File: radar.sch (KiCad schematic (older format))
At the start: 4 parts

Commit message: Schematic finished
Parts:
- added C101, C104, C108, C110, C113: 10u, symbol C_Small
- added C102, C103, C105, C109, C111: 0u1, symbol C_Small
- added C106, C107: 22u, symbol C_Small
- added C112: 47u, symbol C_Small
- added J101, J102, J103, J104, J105: Conn_01x01, symbol Conn_01x01
- added J106, J107: Conn_01x02, symbol Conn_01x02
- added L101: 100u, symbol L_Small
- added R101: DNC, symbol R_Small
- added R102, R103: R_Small, symbol R_Small
- added U101: ADP150AUJZ-1.8-R7, symbol ADP150AUJZ-1.8-R7
- added U102: LM7805_TO220, TO_SOT_Packages_THT:TO-220_Vertical, symbol LM7805_TO220
- added U103: L78L33ABU, symbol L78L33ABU
- added U104: TPS54308, symbol TPS54308
- added U105: L4940D2T12-TR, symbol L4940D2T12-TR
- gave numbers to parts that had none: 4
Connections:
- net +12VA: now also C110.1, C111.1, R101.2, U105.3 (OUT)
- net +3V3: now also C104.1, C105.1, U101.1 (VIN), U101.3 (EN), U103.1 (VOUT)
- net +5V: now also C108.1, C109.1, U102.3 (VO)
- net +BATT: now also C112.1, C113.1, J107.1 (Pin_1), R101.1, U104.3 (VIN), U105.1 (IN)
- net BASEBAND/OUT: now also J105.1 (Pin_1)
- net POWER_AMP/EN: now also J103.1 (Pin_1)
- net POWER_AMP/PDET: now also J102.1 (Pin_1)
- net VCO/TUNE: now also J101.1 (Pin_1)
- net VCO/nEN: now also J104.1 (Pin_1)
- new net: C103.2, L101.1, U104.2 (SW)
- new net: R102.2, R103.1, U104.4 (FB)
- new net: C103.1, U104.6 (BOOT)
- new net: C106.1, C107.1, L101.2, R102.1, U102.1 (VI), U103.3 (VIN)
- new net +1V8: C101.1, C102.1, U101.5 (VOUT)
- new net GND: C101.2, C102.2, C104.2, C105.2, C106.2, C107.2, C108.2, C109.2, C110.2, C111.2, C112.2, C113.2, J107.2 (Pin_2), R103.2, U101.2 (GND), U102.2 (GND), U103.2 (GND), U104.1 (GND), U105.2 (GND)
- new net LEVELSHIFTER/IN1: J106.1 (Pin_1)
- new net LEVELSHIFTER/IN2: J106.2 (Pin_2)
- no-connect marks 0 -> 1
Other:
- note added: "0.7 A RMS, 0.75 A peak\n"
- moved on the sheet: AE101, AE102, T101, T102

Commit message: Assign a lot of footprints, fix l78l33abu part (input and output were reversed)
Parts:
- removed AE101, AE102: Antenna, symbol Antenna
- removed T101, T102: taper, symbol taper
- added J108, J109: Conn_Coaxial, symbol Conn_Coaxial
- C101, C104, C108, C110, C113: footprint (none) -> Capacitors_SMD:C_0805_HandSoldering
- C102, C103, C105, C109, C111: footprint (none) -> Capacitors_SMD:C_0603_HandSoldering
- C106, C107: footprint (none) -> Capacitors_SMD:C_1210_HandSoldering
- J101, J102, J103, J104, J105: footprint (none) -> Connectors:1pin
- J106, J107: footprint (none) -> Socket_Strips:Socket_Strip_Straight_1x02_Pitch2.54mm
- R101: footprint (none) -> Resistors_SMD:R_1206_HandSoldering
- R102: value R_Small -> 100k; footprint (none) -> Resistors_SMD:R_0402
- R103: value R_Small -> 10k; footprint (none) -> Resistors_SMD:R_0603_HandSoldering
- U101: footprint (none) -> rajsradar:TSOT-23
- U103: footprint (none) -> TO_SOT_Packages_SMD:SOT-89-3_Handsoldering
- U104: footprint (none) -> rajsradar:TI-SOT-23-6
- U105: footprint (none) -> rajsradar:D2PAK
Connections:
- net GND: now also J109.2 (Ext)
- net INPUT_AMP/RF_IN: now also J109.1 (In)
- net POWER_AMP/OUT: now also J108.1 (In)
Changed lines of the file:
@@
 Text Notes 6200 650  0    60   ~ 0
 +32 dB, 5V 600mA, max VSWR 4:1
-$Comp
-L Antenna AE101
-U 1 1 59D579C7
-P 8440 790
-F 0 "AE101" H 8365 865 50  0000 R CNN
-F 1 "Antenna" H 8365 790 50  0000 R CNN
-F 2 "" H 8440 790 50  0001 C CNN
-F 3 "" H 8440 790 50  0001 C CNN
-	1    8440 790
-	1    0    0    -1
-$EndComp
-$Comp
-L taper T101
-U 1 1 59D57BA6
-P 8000 1190
-F 0 "T101" H 8000 1340 60  0000 C CNN
-F 1 "taper" H 7900 1040 60  0000 C CNN
-F 2 "" H 8000 1190 60  0001 C CNN
-F 3 "" H 8000 1190 60  0001 C CNN
-	1    8000 1190
-	-1   0    0    1
-$EndComp
 $Sheet
 S 6240 1840 1130 1260
@@
 F4 "OUT" I R 9000 2410 60
 $EndSheet
-$Comp
-L Antenna AE102
-U 1 1 59D63482
-P 2020 2410
-F 0 "AE102" H 1945 2485 50  0000 R CNN
-F 1 "Antenna" H 1945 2410 50  0000 R CNN
-F 2 "" H 2020 2410 50  0001 C CNN
-F 3 "" H 2020 2410 50  0001 C CNN
-	1    2020 2410
-	-1   0    0    -1
-$EndComp
-$Comp
-L taper T102
-U 1 1 59D63488
-P 2460 2810
-F 0 "T102" H 2460 2960 60  0000 C CNN
-F 1 "taper" H 2360 2660 60  0000 C CNN
-F 2 "" H 2460 2810 60  0001 C CNN
-F 3 "" H 2460 2810 60  0001 C CNN
-	1    2460 2810
-	1    0    0    1
-$EndComp
 Text Notes 6360 3290 0    60   ~ 0
 +0 dB, 5V 60mA
@@
 F 0 "R101" H 2150 4880 50  0000 L CNN
 F 1 "DNC" H 2150 4820 50  0000 L CNN
-F 2 "" H 2120 4860 50  0001 C CNN
+F 2 "Resistors_SMD:R_1206_HandSoldering" H 2120 4860 50  0001 C CNN
 F 3 "" H 2120 4860 50  0001 C CNN
 	1    2120 4860
@@
 F 0 "U105" H 2130 5170 60  0000 C CNN
 F 1 "L4940D2T12-TR" H 2130 5320 60  0000 C CNN
-F 2 "" H 2130 5170 60  0001 C CNN
+F 2 "rajsradar:D2PAK" H 2130 5170 60  0001 C CNN
 F 3 "" H 2130 5170 60  0001 C CNN
 	1    2130 5170
@@
 F 0 "U104" H 3890 4900 60  0000 C CNN
 F 1 "TPS54308" H 3890 5200 60  0000 C CNN
-F 2 "" H 3890 4900 60  0001 C CNN
+F 2 "rajsradar:TI-SOT-23-6" H 3890 4900 60  0001 C CNN
 F 3 "" H 3890 4900 60  0001 C CNN
 	1    3890 4900
@@
 F 0 "C103" H 4630 4820 50  0000 L CNN
 F 1 "0u1" H 4630 4670 50  0000 L CNN
-F 2 "" H 4620 4750 50  0001 C CNN
+F 2 "Capacitors_SMD:C_0603_HandSoldering" H 4620 4750 50  0001 C CNN
 F 3 "" H 4620 4750 50  0001 C CNN
 	1    4620 4750
@@
 F 0 "C106" H 5090 5110 50  0000 L CNN
 F 1 "22u" H 5090 4960 50  0000 L CNN
-F 2 "" H 5080 5040 50  0001 C CNN
+F 2 "Capacitors_SMD:C_1210_HandSoldering" H 5080 5040 50  0001 C CNN
 F 3 "" H 5080 5040 50  0001 C CNN
 	1    5080 5040
@@
 F 0 "C107" H 5300 5110 50  0000 L CNN
 F 1 "22u" H 5300 4960 50  0000 L CNN
-F 2 "" H 5290 5040 50  0001 C CNN
+F 2 "Capacitors_SMD:C_1210_HandSoldering" H 5290 5040 50  0001 C CNN
 F 3 "" H 5290 5040 50  0001 C CNN
 	1    5290 5040
@@
 P 5540 5050
 F 0 "R102" H 5570 5070 50  0000 L CNN
-F 1 "R_Small" H 5570 5010 50  0000 L CNN
-F 2 "" H 5540 5050 50  0001 C CNN
+F 1 "100k" H 5570 5010 50  0000 L CNN
+F 2 "Resistors_SMD:R_0402" H 5540 5050 50  0001 C CNN
 F 3 "" H 5540 5050 50  0001 C CNN
 	1    5540 5050
@@
 P 5540 5300
 F 0 "R103" H 5570 5320 50  0000 L CNN
-F 1 "R_Small" H 5570 5260 50  0000 L CNN
-F 2 "" H 5540 5300 50  0001 C CNN
+F 1 "10k" H 5570 5260 50  0000 L CNN
+F 2 "Resistors_SMD:R_0603_HandSoldering" H 5540 5300 50  0001 C CNN
 F 3 "" H 5540 5300 50  0001 C CNN
 	1    5540 5300
@@
 F 0 "C110" H 2770 5410 50  0000 L CNN
 F 1 "10u" H 2770 5260 50  0000 L CNN
-F 2 "" H 2760 5340 50  0001 C CNN
+F 2 "Capacitors_SMD:C_0805_HandSoldering" H 2760 5340 50  0001 C CNN
 F 3 "" H 2760 5340 50  0001 C CNN
 	1    2760 5340
@@
 F 0 "C111" H 2980 5410 50  0000 L CNN
 F 1 "0u1" H 2980 5260 50  0000 L CNN
-F 2 "" H 2970 5340 50  0001 C CNN
+F 2 "Capacitors_SMD:C_0603_HandSoldering" H 2970 5340 50  0001 C CNN
 F 3 "" H 2970 5340 50  0001 C CNN
 	1    2970 5340
@@
 F 0 "C113" H 1550 5440 50  0000 L CNN
 F 1 "10u" H 1550 5290 50  0000 L CNN
-F 2 "" H 1540 5370 50  0001 C CNN
+F 2 "Capacitors_SMD:C_0805_HandSoldering" H 1540 5370 50  0001 C CNN
 F 3 "" H 1540 5370 50  0001 C CNN
 	1    1540 5370
@@
 F 0 "U103" H 7250 4780 60  0000 C CNN
 F 1 "L78L33ABU" H 7250 4880 60  0000 C CNN
-F 2 "" H 7250 4630 60  0001 C CNN
+F 2 "TO_SOT_Packages_SMD:SOT-89-3_Handsoldering" H 7250 4630 60  0001 C CNN
 F 3 "" H 7250 4630 60  0001 C CNN
 	1    7250 4630
@@
 F 0 "U101" H 8880 4480 60  0000 C CNN
 F 1 "ADP150AUJZ-1.8-R7" H 8880 4680 60  0000 C CNN
-F 2 "" H 8880 4480 60  0001 C CNN
+F 2 "rajsradar:TSOT-23" H 8880 4480 60  0001 C CNN
 F 3 "" H 8880 4480 60  0001 C CNN
 	1    8880 4480
@@
 F 0 "C108" H 6410 5160 50  0000 L CNN
 F 1 "10u" H 6410 5010 50  0000 L CNN
-F 2 "" H 6400 5090 50  0001 C CNN
+F 2 "Capacitors_SMD:C_0805_HandSoldering" H 6400 5090 50  0001 C CNN
 F 3 "" H 6400 5090 50  0001 C CNN
 	1    6400 5090
@@
 F 0 "C109" H 6620 5160 50  0000 L CNN
 F 1 "0u1" H 6620 5010 50  0000 L CNN
-F 2 "" H 6610 5090 50  0001 C CNN
+F 2 "Capacitors_SMD:C_0603_HandSoldering" H 6610 5090 50  0001 C CNN
 F 3 "" H 6610 5090 50  0001 C CNN
 	1    6610 5090
@@
 F 0 "C104" H 7790 4870 50  0000 L CNN
 F 1 "10u" H 7790 4720 50  0000 L CNN
-F 2 "" H 7780 4800 50  0001 C CNN
+F 2 "Capacitors_SMD:C_0805_HandSoldering" H 7780 4800 50  0001 C CNN
 F 3 "" H 7780 4800 50  0001 C CNN
 	1    7780 4800
@@
 F 0 "C105" H 8000 4870 50  0000 L CNN
 F 1 "0u1" H 8000 4720 50  0000 L CNN
-F 2 "" H 7990 4800 50  0001 C CNN
+F 2 "Capacitors_SMD:C_0603_HandSoldering" H 7990 4800 50  0001 C CNN
 F 3 "" H 7990 4800 50  0001 C CNN
 	1    7990 4800
@@
 F 0 "C101" H 9570 4670 50  0000 L CNN
 F 1 "10u" H 9570 4520 50  0000 L CNN
-F 2 "" H 9560 4600 50  0001 C CNN
+F 2 "Capacitors_SMD:C_0805_HandSoldering" H 9560 4600 50  0001 C CNN
 F 3 "" H 9560 4600 50  0001 C CNN
 	1    9560 4600
@@
 F 0 "C102" H 9780 4670 50  0000 L CNN
 F 1 "0u1" H 9780 4520 50  0000 L CNN
-F 2 "" H 9770 4600 50  0001 C CNN
+F 2 "Capacitors_SMD:C_0603_HandSoldering" H 9770 4600 50  0001 C CNN
 F 3 "" H 9770 4600 50  0001 C CNN
 	1    9770 4600
@@
 	5380 2790 6240 2790
 Wire Wire Line
-	2760 2810 3200 2810
-Wire Wire Line
-	2020 2810 2160 2810
-Wire Wire Line
-	2020 2610 2020 2810
+	1740 2470 3200 2470
 Wire Wire Line
 	5520 1930 6240 1930
 Wire Wire Line
-	7700 1190 7370 1190
-Wire Wire Line
-	8440 1190 8300 1190
-Wire Wire Line
-	8440 990  8440 1190
+	7370 1190 8440 1190
 Wire Wire Line
 	5520 1260 6240 1260
@@
 $EndSheet
 Wire Wire Line
-	3200 2810 3200 3100
+	3200 2470 3200 3100
 Wire Wire Line
 	3200 3100 3290 3100
@@
 F 0 "J106" H 1010 3480 50  0000 C CNN
 F 1 "Conn_01x02" H 1010 3180 50  0000 C CNN
-F 2 "" H 1010 3380 50  0001 C CNN
+F 2 "Socket_Strips:Socket_Strip_Straight_1x02_Pitch2.54mm" H 1010 3380 50  0001 C CNN
 F 3 "" H 1010 3380 50  0001 C CNN
 	1    1010 3380
@@
 F 0 "J104" H 2620 1820 50  0000 C CNN
 F 1 "Conn_01x01" H 2620 1620 50  0000 C CNN
-F 2 "" H 2620 1720 50  0001 C CNN
+F 2 "Connectors:1pin" H 2620 1720 50  0001 C CNN
 F 3 "" H 2620 1720 50  0001 C CNN
 	1    2620 1720
@@
 F 0 "J101" H 2600 1390 50  0000 C CNN
 F 1 "Conn_01x01" H 2600 1190 50  0000 C CNN
-F 2 "" H 2600 1290 50  0001 C CNN
+F 2 "Connectors:1pin" H 2600 1290 50  0001 C CNN
 F 3 "" H 2600 1290 50  0001 C CNN
 	1    2600 1290
@@
 F 0 "J103" H 5810 1550 50  0000 C CNN
 F 1 "Conn_01x01" H 5810 1350 50  0000 C CNN
-F 2 "" H 5810 1450 50  0001 C CNN
+F 2 "Connectors:1pin" H 5810 1450 50  0001 C CNN
 F 3 "" H 5810 1450 50  0001 C CNN
 	1    5810 1450
@@
 F 0 "J102" H 7720 1520 50  0000 C CNN
 F 1 "Conn_01x01" H 7720 1320 50  0000 C CNN
-F 2 "" H 7720 1420 50  0001 C CNN
+F 2 "Connectors:1pin" H 7720 1420 50  0001 C CNN
 F 3 "" H 7720 1420 50  0001 C CNN
 	1    7720 1420
@@
 F 0 "J105" H 9330 2510 50  0000 C CNN
 F 1 "Conn_01x01" H 9330 2310 50  0000 C CNN
-F 2 "" H 9330 2410 50  0001 C CNN
+F 2 "Connectors:1pin" H 9330 2410 50  0001 C CNN
 F 3 "" H 9330 2410 50  0001 C CNN
 	1    9330 2410
@@
 F 0 "J107" H 700 4740 50  0000 C CNN
 F 1 "Conn_01x02" H 700 4440 50  0000 C CNN
-F 2 "" H 700 4640 50  0001 C CNN
+F 2 "Socket_Strips:Socket_Strip_Straight_1x02_Pitch2.54mm" H 700 4640 50  0001 C CNN
 F 3 "" H 700 4640 50  0001 C CNN
 	1    700  4640
@@
 Wire Wire Line
 	1020 4740 900  4740
+$Comp
+L Conn_Coaxial J109
+U 1 1 5A5A7286
+P 1590 2470
+F 0 "J109" H 1600 2590 50  0000 C CNN
+F 1 "Conn_Coaxial" V 1705 2470 50  0000 C CNN
+F 2 "" H 1590 2470 50  0001 C CNN
+F 3 "" H 1590 2470 50  0001 C CNN
+	1    1590 2470
+	-1   0    0    -1
+$EndComp
+$Comp
+L Conn_Coaxial J108
+U 1 1 5A5A73C3
+P 8590 1190
+F 0 "J108" H 8600 1310 50  0000 C CNN
+F 1 "Conn_Coaxial" V 8705 1190 50  0000 C CNN
+F 2 "" H 8590 1190 50  0001 C CNN
+F 3 "" H 8590 1190 50  0001 C CNN
+	1    8590 1190
+	1    0    0    -1
+$EndComp
+$Comp
+L GND #PWR025
+U 1 1 5A5A8BA4
+P 1590 2760
+F 0 "#PWR025" H 1590 2510 50  0001 C CNN
+F 1 "GND" H 1590 2610 50  0000 C CNN
+F 2 "" H 1590 2760 50  0001 C CNN
+F 3 "" H 1590 2760 50  0001 C CNN
+	1    1590 2760
+	1    0    0    -1
+$EndComp
+Wire Wire Line
+	1590 2670 1590 2760
 $EndSCHEMATC

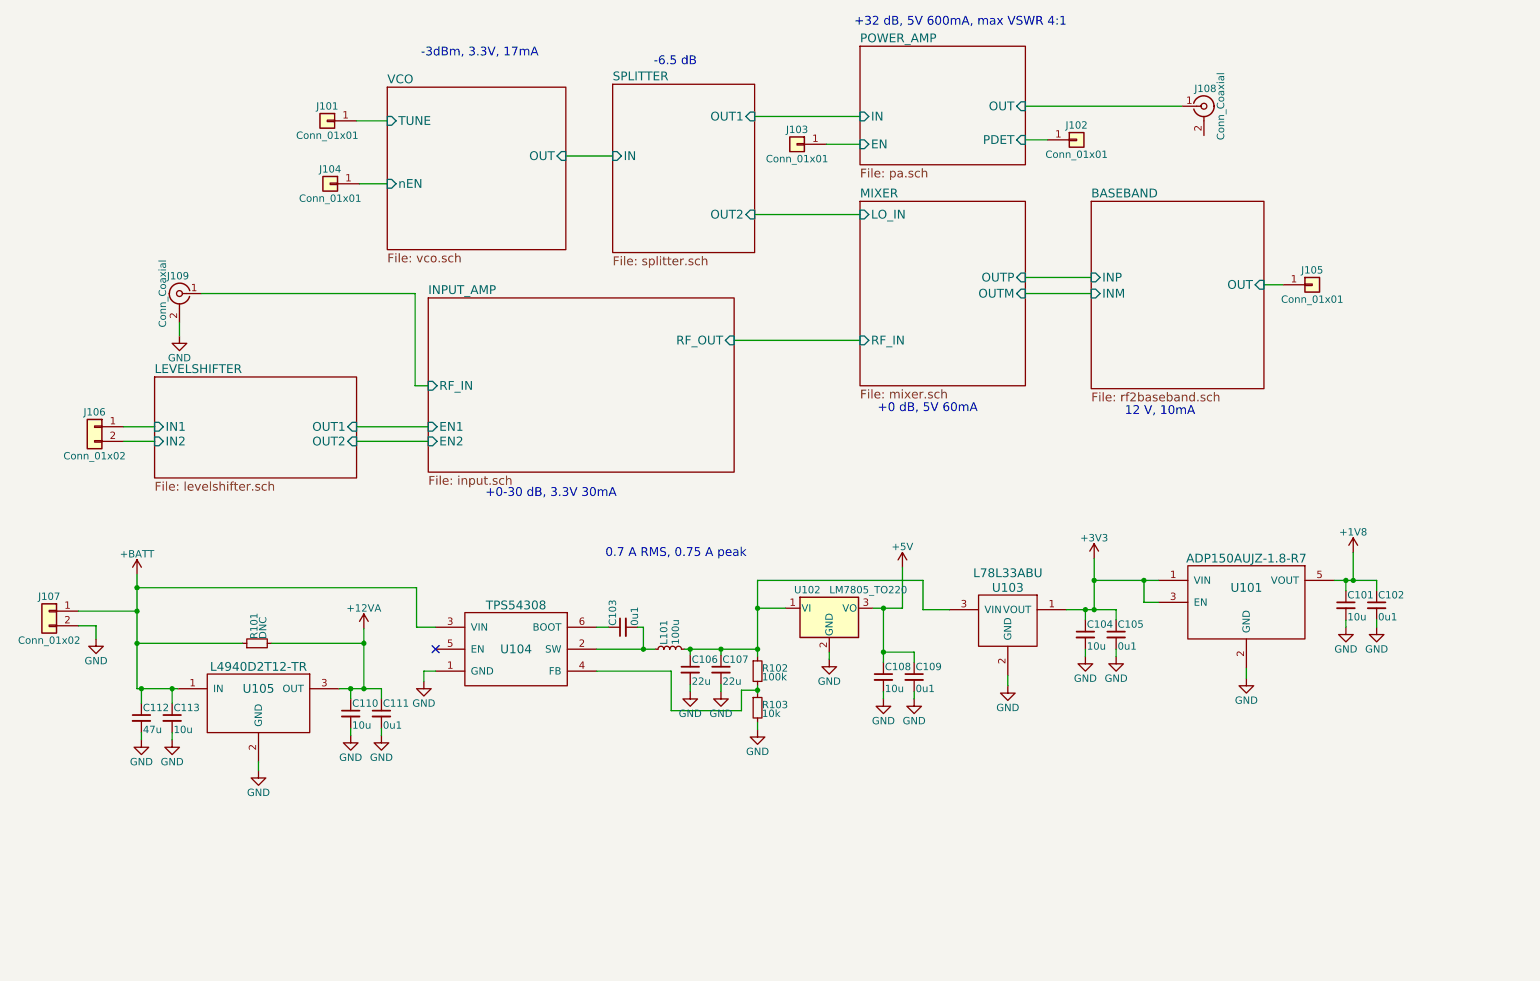
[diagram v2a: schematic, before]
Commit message: Finished circuit layout (for the RF board)
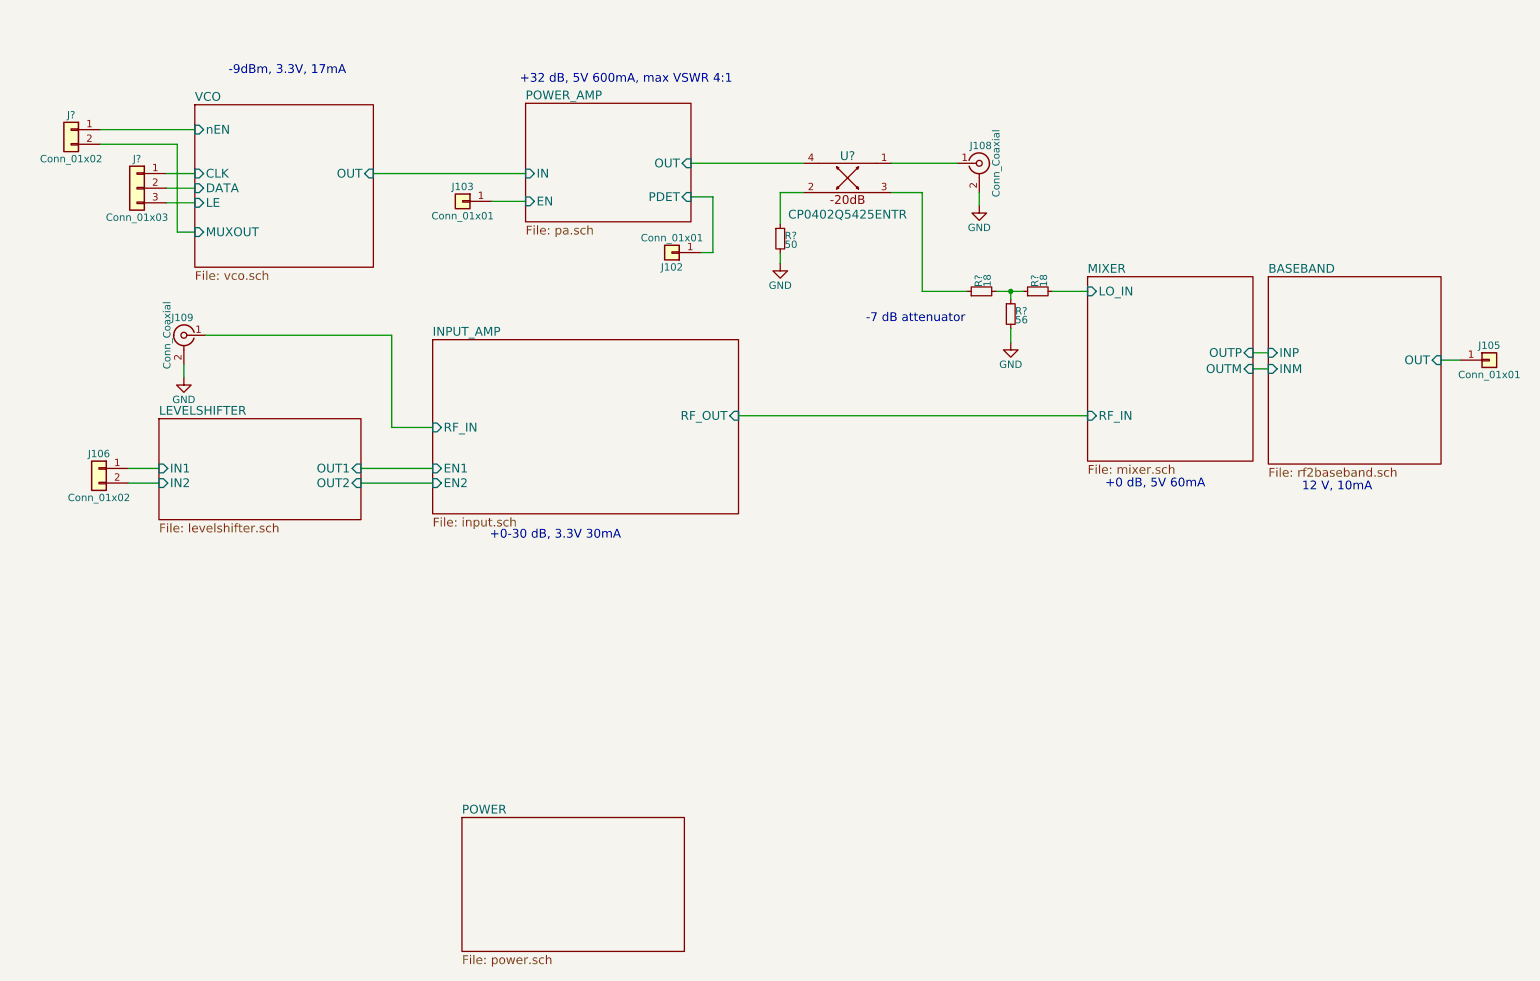
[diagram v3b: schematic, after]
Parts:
- removed C101, C104, C108, C110, C113: 10u, Capacitors_SMD:C_0805_HandSoldering, symbol C_Small
- removed C102, C103, C105, C109, C111: 0u1, Capacitors_SMD:C_0603_HandSoldering, symbol C_Small
- removed C106, C107: 22u, Capacitors_SMD:C_1210_HandSoldering, symbol C_Small
- removed C112: 47u, symbol C_Small
- removed J101, J104: Conn_01x01, Connectors:1pin, symbol Conn_01x01
- removed J107: Conn_01x02, Socket_Strips:Socket_Strip_Straight_1x02_Pitch2.54mm, symbol Conn_01x02
- removed L101: 100u, symbol L_Small
- removed R101: DNC, Resistors_SMD:R_1206_HandSoldering, symbol R_Small
- removed R102: 100k, Resistors_SMD:R_0402, symbol R_Small
- removed R103: 10k, Resistors_SMD:R_0603_HandSoldering, symbol R_Small
- removed U101: ADP150AUJZ-1.8-R7, rajsradar:TSOT-23, symbol ADP150AUJZ-1.8-R7
- removed U102: LM7805_TO220, TO_SOT_Packages_THT:TO-220_Vertical, symbol LM7805_TO220
- removed U103: L78L33ABU, TO_SOT_Packages_SMD:SOT-89-3_Handsoldering, symbol L78L33ABU
- removed U104: TPS54308, rajsradar:TI-SOT-23-6, symbol TPS54308
- removed U105: L4940D2T12-TR, rajsradar:D2PAK, symbol L4940D2T12-TR
- added J?: Conn_01x03, symbol Conn_01x03
- added J?: Conn_01x02, symbol Conn_01x02
- added R?: 50, symbol R_Small
- added R? (x2): 18, symbol R_Small
- added R?: 56, symbol R_Small
- added U?: CP0402Q5425ENTR, symbol CP0402Q5425ENTR
- J108, J109: footprint (none) -> rajsradar:132322
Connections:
- net GND: now also J108.2 (Ext), R?.2, R?.2
- net MIXER/LO_IN: now also R?.2
- net POWER_AMP/OUT: now also U?.4; no longer J108.1 (In)
- net VCO/nEN: now also J?.1 (Pin_1)
- new net: J108.1 (In), U?.1
- new net: R?.1, U?.2
- new net: R?.1, U?.3
- new net: R?.1, R?.1, R?.2
- new net VCO/CLK: J?.1 (Pin_1)
- new net VCO/DATA: J?.2 (Pin_2)
- new net VCO/LE: J?.3 (Pin_3)
- new net VCO/MUXOUT: J?.2 (Pin_2)
- no-connect marks 1 -> 0
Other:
- note added: "-7 dB attenuator"
- note added: "-9dBm, 3.3V, 17mA"
- note removed: "-3dBm, 3.3V, 17mA"
- note removed: "-6.5 dB"
- note removed: "0.7 A RMS, 0.75 A peak\n"
- moved on the sheet: J102, J103, J105, J106, J108, J109
